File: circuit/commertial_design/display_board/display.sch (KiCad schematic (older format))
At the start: 14 parts, among them P1 CONN_02X03, P5 CONN_01X08, P6 CONN_01X12, SW1 SW_PUSH, SW2 SW_PUSH, SW3 SW_PUSH, U10 IN-14, U11 IN-14, U12 IN-14, U13 IN-14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

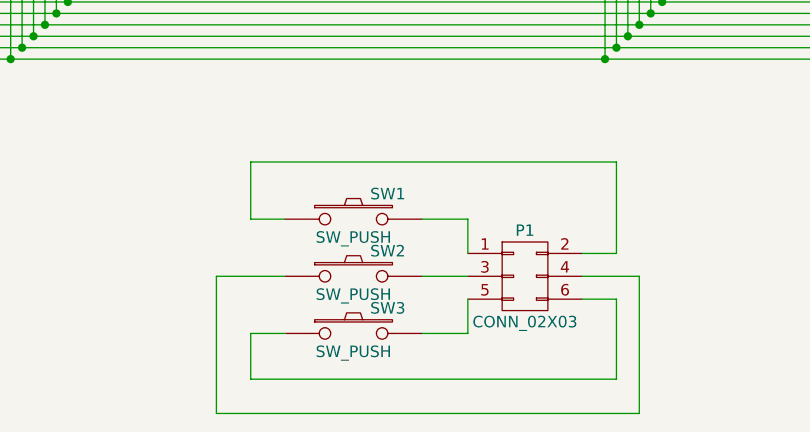
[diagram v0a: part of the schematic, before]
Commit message: Layout need to be arranged, scheme is finished
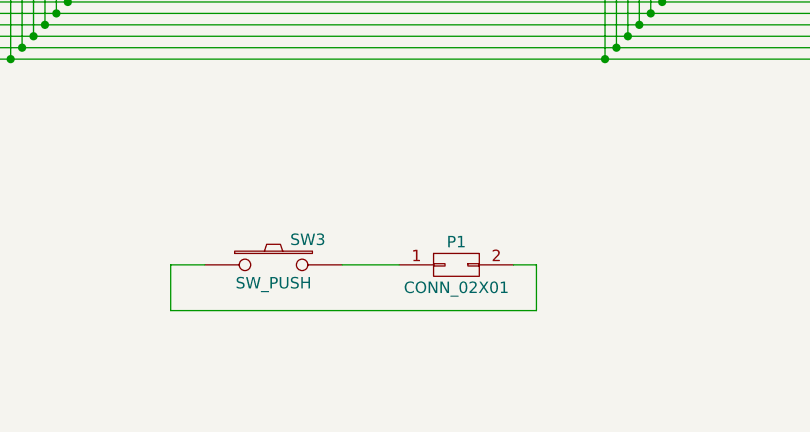
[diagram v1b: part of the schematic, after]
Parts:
- removed P1: CONN_02X03, SMD_PIN_2_BY_3:SMD_PIN_2_BY_3, symbol CONN_02X03
- removed SW1, SW2: SW_PUSH, Buttons_Switches_ThroughHole:SW_PUSH-12mm, symbol SW_PUSH
- added P1: CONN_02X01, Pin_Headers:Pin_Header_Straight_2x01, symbol CONN_02X01
- P5: footprint SMD_PIN_2_BY_4:SMD_PIN_2_BY_4 -> Pin_Headers:Pin_Header_Straight_2x04
- P6: footprint SMD_PIN_2_BY_6:SMD_PIN_2_BY_6 -> Pin_Headers:Pin_Header_Straight_2x06
- U10, U11, U12, U13, U14, U15, U16, U17: footprint IN-14:IN-14 -> IN-14-board:IN-14
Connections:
- net at SW3.1: now also P1.2 (P2)
- net at SW3.2: now also P1.1 (P1)
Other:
- moved on the sheet: SW3
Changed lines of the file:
@@
 F 0 "U10" H 1700 2900 60  0000 C CNN
 F 1 "IN-14" H 2000 2900 60  0000 C CNN
-F 2 "IN-14:IN-14" H 1700 2900 60  0001 C CNN
+F 2 "IN-14-board:IN-14" H 1700 2900 60  0001 C CNN
 F 3 "" H 1700 2900 60  0000 C CNN
 	1    1950 2250
@@
 F 0 "U12" H 4300 2900 60  0000 C CNN
 F 1 "IN-14" H 4600 2900 60  0000 C CNN
-F 2 "IN-14:IN-14" H 4300 2900 60  0001 C CNN
+F 2 "IN-14-board:IN-14" H 4300 2900 60  0001 C CNN
 F 3 "" H 4300 2900 60  0000 C CNN
 	1    4550 2250
@@
 F 0 "U14" H 6900 2900 60  0000 C CNN
 F 1 "IN-14" H 7200 2900 60  0000 C CNN
-F 2 "IN-14:IN-14" H 6900 2900 60  0001 C CNN
+F 2 "IN-14-board:IN-14" H 6900 2900 60  0001 C CNN
 F 3 "" H 6900 2900 60  0000 C CNN
 	1    7150 2250
@@
 F 0 "U16" H 9500 2900 60  0000 C CNN
 F 1 "IN-14" H 9800 2900 60  0000 C CNN
-F 2 "IN-14:IN-14" H 9500 2900 60  0001 C CNN
+F 2 "IN-14-board:IN-14" H 9500 2900 60  0001 C CNN
 F 3 "" H 9500 2900 60  0000 C CNN
 	1    9750 2250
@@
 F 0 "U11" H 1700 5650 60  0000 C CNN
 F 1 "IN-14" H 2000 5650 60  0000 C CNN
-F 2 "IN-14:IN-14" H 1700 5650 60  0001 C CNN
+F 2 "IN-14-board:IN-14" H 1700 5650 60  0001 C CNN
 F 3 "" H 1700 5650 60  0000 C CNN
 	1    1950 5000
@@
 F 0 "U13" H 4300 5650 60  0000 C CNN
 F 1 "IN-14" H 4600 5650 60  0000 C CNN
-F 2 "IN-14:IN-14" H 4300 5650 60  0001 C CNN
+F 2 "IN-14-board:IN-14" H 4300 5650 60  0001 C CNN
 F 3 "" H 4300 5650 60  0000 C CNN
 	1    4550 5000
@@
 F 0 "U15" H 6900 5650 60  0000 C CNN
 F 1 "IN-14" H 7200 5650 60  0000 C CNN
-F 2 "IN-14:IN-14" H 6900 5650 60  0001 C CNN
+F 2 "IN-14-board:IN-14" H 6900 5650 60  0001 C CNN
 F 3 "" H 6900 5650 60  0000 C CNN
 	1    7150 5000
@@
 F 0 "U17" H 9500 5650 60  0000 C CNN
 F 1 "IN-14" H 9800 5650 60  0000 C CNN
-F 2 "IN-14:IN-14" H 9500 5650 60  0001 C CNN
+F 2 "IN-14-board:IN-14" H 9500 5650 60  0001 C CNN
 F 3 "" H 9500 5650 60  0000 C CNN
 	1    9750 5000
@@
 F 0 "P5" H 1100 7150 50  0000 C CNN
 F 1 "CONN_01X08" V 1200 6700 50  0000 C CNN
-F 2 "SMD_PIN_2_BY_4:SMD_PIN_2_BY_4" H 1100 6700 50  0001 C CNN
+F 2 "Pin_Headers:Pin_Header_Straight_2x04" H 1100 6700 50  0001 C CNN
 F 3 "" H 1100 6700 50  0000 C CNN
 	1    1100 6700
@@
 F 0 "P6" H 1950 7350 50  0000 C CNN
 F 1 "CONN_01X12" V 2050 6700 50  0000 C CNN
-F 2 "SMD_PIN_2_BY_6:SMD_PIN_2_BY_6" H 1950 6700 50  0001 C CNN
+F 2 "Pin_Headers:Pin_Header_Straight_2x06" H 1950 6700 50  0001 C CNN
 F 3 "" H 1950 6700 50  0000 C CNN
 	1    1950 6700
@@
 Connection ~ 10700 1750
 $Comp
-L SW_PUSH SW1
-U 1 1 573D27B7
-P 4850 6550
-F 0 "SW1" H 5000 6660 50  0000 C CNN
-F 1 "SW_PUSH" H 4850 6470 50  0000 C CNN
-F 2 "Buttons_Switches_ThroughHole:SW_PUSH-12mm" H 4850 6550 50  0001 C CNN
-F 3 "" H 4850 6550 50  0000 C CNN
-	1    4850 6550
-	1    0    0    -1
-$EndComp
-$Comp
-L SW_PUSH SW2
-U 1 1 573D2802
-P 4850 6800
-F 0 "SW2" H 5000 6910 50  0000 C CNN
-F 1 "SW_PUSH" H 4850 6720 50  0000 C CNN
-F 2 "Buttons_Switches_ThroughHole:SW_PUSH-12mm" H 4850 6800 50  0001 C CNN
-F 3 "" H 4850 6800 50  0000 C CNN
-	1    4850 6800
-	1    0    0    -1
-$EndComp
-$Comp
 L SW_PUSH SW3
 U 1 1 573D2843
-P 4850 7050
-F 0 "SW3" H 5000 7160 50  0000 C CNN
-F 1 "SW_PUSH" H 4850 6970 50  0000 C CNN
-F 2 "Buttons_Switches_ThroughHole:SW_PUSH-12mm" H 4850 7050 50  0001 C CNN
-F 3 "" H 4850 7050 50  0000 C CNN
-	1    4850 7050
-	1    0    0    -1
-$EndComp
-$Comp
-L CONN_02X03 P1
-U 1 1 573D2ACB
-P 5600 6800
-F 0 "P1" H 5600 7000 50  0000 C CNN
-F 1 "CONN_02X03" H 5600 6600 50  0000 C CNN
-F 2 "SMD_PIN_2_BY_3:SMD_PIN_2_BY_3" H 5600 5600 50  0001 C CNN
-F 3 "" H 5600 5600 50  0000 C CNN
-	1    5600 6800
-	1    0    0    -1
-$EndComp
-Wire Wire Line
-	5150 6800 5350 6800
-Wire Wire Line
-	5150 6550 5350 6550
-Wire Wire Line
-	5350 6550 5350 6700
-Wire Wire Line
-	5150 7050 5350 7050
-Wire Wire Line
-	5350 7050 5350 6900
-Wire Wire Line
-	5850 6700 6000 6700
-Wire Wire Line
-	6000 6700 6000 6300
-Wire Wire Line
-	6000 6300 4400 6300
-Wire Wire Line
-	4400 6300 4400 6550
-Wire Wire Line
-	4400 6550 4550 6550
-Wire Wire Line
-	5850 6900 6000 6900
-Wire Wire Line
-	6000 6900 6000 7250
-Wire Wire Line
-	6000 7250 4400 7250
-Wire Wire Line
-	4400 7250 4400 7050
-Wire Wire Line
-	4400 7050 4550 7050
-Wire Wire Line
-	5850 6800 6100 6800
-Wire Wire Line
-	6100 6800 6100 7400
-Wire Wire Line
-	6100 7400 4250 7400
-Wire Wire Line
-	4250 7400 4250 6800
-Wire Wire Line
-	4250 6800 4550 6800
+P 4500 6750
+F 0 "SW3" H 4650 6860 50  0000 C CNN
+F 1 "SW_PUSH" H 4500 6670 50  0000 C CNN
+F 2 "Buttons_Switches_ThroughHole:SW_PUSH-12mm" H 4500 6750 50  0001 C CNN
+F 3 "" H 4500 6750 50  0000 C CNN
+	1    4500 6750
+	1    0    0    -1
+$EndComp
+Wire Wire Line
+	4800 6750 5050 6750
+Wire Wire Line
+	5650 6950 4050 6950
+Wire Wire Line
+	4050 6950 4050 6750
+Wire Wire Line
+	4050 6750 4200 6750
+$Comp
+L CONN_02X01 P1
+U 1 1 57A4B8DF
+P 5300 6750
+F 0 "P1" H 5300 6850 50  0000 C CNN
+F 1 "CONN_02X01" H 5300 6650 50  0000 C CNN
+F 2 "Pin_Headers:Pin_Header_Straight_2x01" H 5300 5550 50  0001 C CNN
+F 3 "" H 5300 5550 50  0000 C CNN
+	1    5300 6750
+	1    0    0    -1
+$EndComp
+Wire Wire Line
+	5550 6750 5650 6750
+Wire Wire Line
+	5650 6750 5650 6950
 $EndSCHEMATC

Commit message: Fix display board button
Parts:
- SW3: footprint Buttons_Switches_ThroughHole:SW_PUSH-12mm -> button:SW_PUSH-12mm
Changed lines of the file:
@@
 F 0 "SW3" H 4650 6860 50  0000 C CNN
 F 1 "SW_PUSH" H 4500 6670 50  0000 C CNN
-F 2 "Buttons_Switches_ThroughHole:SW_PUSH-12mm" H 4500 6750 50  0001 C CNN
+F 2 "button:SW_PUSH-12mm" H 4500 6750 50  0001 C CNN
 F 3 "" H 4500 6750 50  0000 C CNN
 	1    4500 6750
